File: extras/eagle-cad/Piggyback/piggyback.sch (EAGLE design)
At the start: 2 parts

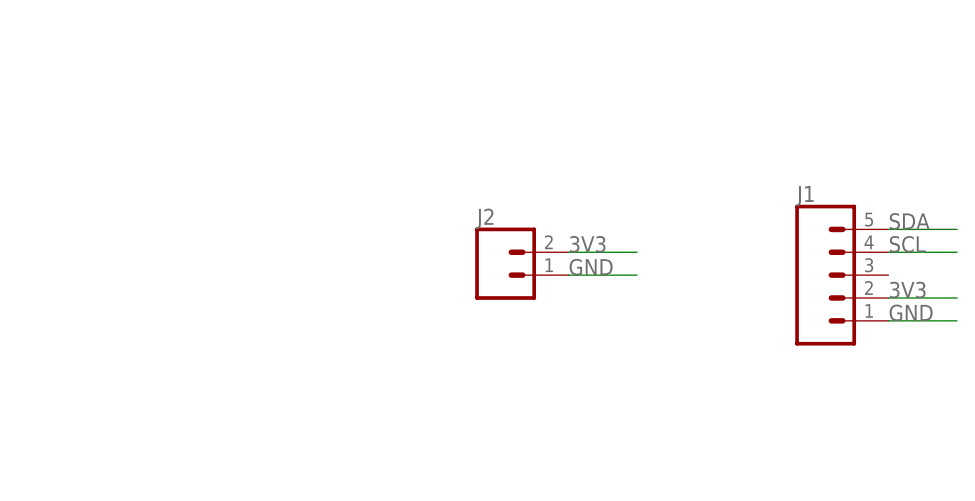
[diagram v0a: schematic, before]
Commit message: Added RX to piggyback board [Issue 134]
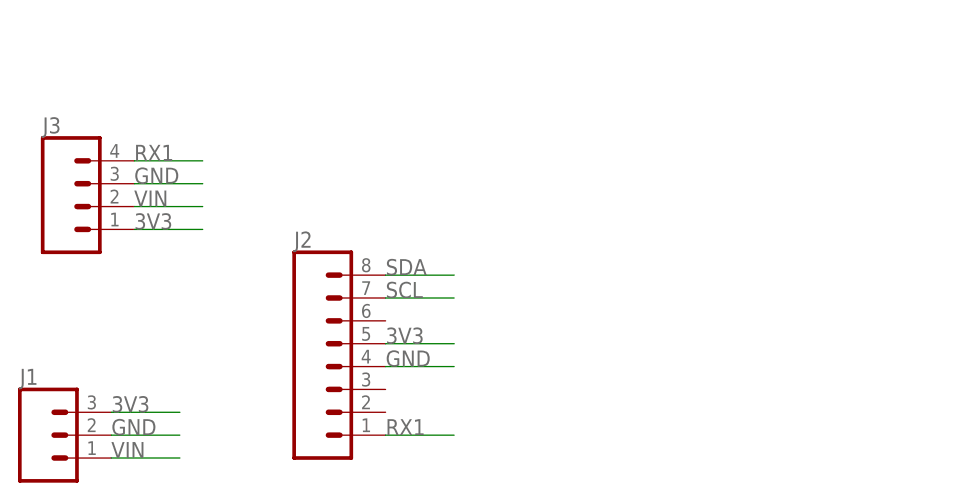
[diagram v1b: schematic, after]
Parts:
- added J3: (no value), SparkFun-Connectors:CONN_041X04_NO_SILK
- J1: device SparkFun-Connectors:CONN_05NO_SILK -> SparkFun-Connectors:CONN_031X03_NO_SILK
- J2: device SparkFun-Connectors:CONN_021X02_NO_SILK -> SparkFun-Connectors:CONN_08NO_SILK_FEMALE_PTH
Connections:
- new net RX1: J2.1, J3.4
- new net VIN: J1.1, J3.2
- net 3V3: now also J1.3, J2.5, J3.1; no longer J1.2, J2.2
- net GND: now also J1.2, J2.4, J3.3; no longer J1.1, J2.1
- net SCL: now also J2.7; no longer J1.4
- net SDA: now also J2.8; no longer J1.5
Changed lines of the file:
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@@
 </classes>
 <parts>
-<part name="J2" library="SparkFun-Connectors" deviceset="CONN_02" device="1X02_NO_SILK"/>
-<part name="J1" library="SparkFun-Connectors" deviceset="CONN_05" device="NO_SILK"/>
+<part name="J1" library="SparkFun-Connectors" deviceset="CONN_03" device="1X03_NO_SILK"/>
+<part name="J2" library="SparkFun-Connectors" deviceset="CONN_08" device="NO_SILK_FEMALE_PTH"/>
+<part name="J3" library="SparkFun-Connectors" deviceset="CONN_04" device="1X04_NO_SILK"/>
 </parts>
 <sheets>
@@
 </plain>
 <instances>
-<instance part="J2" gate="G$1" x="-68.58" y="15.24" smashed="yes">
-<attribute name="VALUE" x="-71.12" y="10.414" size="1.778" layer="96" font="vector"/>
-<attribute name="NAME" x="-71.12" y="20.828" size="1.778" layer="95" font="vector"/>
+<instance part="J1" gate="J$1" x="-119.38" y="-2.54" smashed="yes">
+<attribute name="VALUE" x="-121.92" y="-9.906" size="1.778" layer="96" font="vector"/>
+<attribute name="NAME" x="-121.92" y="3.048" size="1.778" layer="95" font="vector"/>
 </instance>
-<instance part="J1" gate="G$1" x="-33.02" y="15.24" smashed="yes">
-<attribute name="VALUE" x="-35.56" y="5.334" size="1.778" layer="96" font="vector"/>
-<attribute name="NAME" x="-35.56" y="23.368" size="1.778" layer="95" font="vector"/>
+<instance part="J2" gate="G$1" x="-86.36" y="5.08" smashed="yes">
+<attribute name="VALUE" x="-91.44" y="-7.366" size="1.778" layer="96" font="vector"/>
+<attribute name="NAME" x="-91.44" y="18.288" size="1.778" layer="95" font="vector"/>
+</instance>
+<instance part="J3" gate="J1" x="-114.3" y="22.86" smashed="yes">
+<attribute name="VALUE" x="-119.38" y="15.494" size="1.778" layer="96" font="vector"/>
+<attribute name="NAME" x="-119.38" y="30.988" size="1.778" layer="95" font="vector"/>
 </instance>
 </instances>
@@
 </busses>
 <nets>
+<net name="VIN" class="0">
+<segment>
+<pinref part="J1" gate="J$1" pin="1"/>
+<wire x1="-111.76" y1="-5.08" x2="-104.14" y2="-5.08" width="0.1524" layer="91"/>
+<label x="-111.76" y="-5.08" size="1.778" layer="95"/>
+</segment>
+<segment>
+<pinref part="J3" gate="J1" pin="2"/>
+<wire x1="-109.22" y1="22.86" x2="-101.6" y2="22.86" width="0.1524" layer="91"/>
+<label x="-109.22" y="22.86" size="1.778" layer="95"/>
+</segment>
+</net>
 <net name="GND" class="0">
 <segment>
-<pinref part="J2" gate="G$1" pin="1"/>
-<wire x1="-60.96" y1="15.24" x2="-53.34" y2="15.24" width="0.1524" layer="91"/>
-<label x="-60.96" y="15.24" size="1.778" layer="95"/>
+<pinref part="J1" gate="J$1" pin="2"/>
+<wire x1="-111.76" y1="-2.54" x2="-104.14" y2="-2.54" width="0.1524" layer="91"/>
+<label x="-111.76" y="-2.54" size="1.778" layer="95"/>
 </segment>
 <segment>
-<pinref part="J1" gate="G$1" pin="1"/>
-<wire x1="-25.4" y1="10.16" x2="-17.78" y2="10.16" width="0.1524" layer="91"/>
-<label x="-25.4" y="10.16" size="1.778" layer="95"/>
+<pinref part="J2" gate="G$1" pin="4"/>
+<wire x1="-81.28" y1="5.08" x2="-73.66" y2="5.08" width="0.1524" layer="91"/>
+<label x="-81.28" y="5.08" size="1.778" layer="95"/>
+</segment>
+<segment>
+<pinref part="J3" gate="J1" pin="3"/>
+<wire x1="-109.22" y1="25.4" x2="-101.6" y2="25.4" width="0.1524" layer="91"/>
+<label x="-109.22" y="25.4" size="1.778" layer="95"/>
 </segment>
 </net>
 <net name="3V3" class="0">
 <segment>
-<pinref part="J2" gate="G$1" pin="2"/>
-<wire x1="-60.96" y1="17.78" x2="-53.34" y2="17.78" width="0.1524" layer="91"/>
-<label x="-60.96" y="17.78" size="1.778" layer="95"/>
+<pinref part="J1" gate="J$1" pin="3"/>
+<wire x1="-111.76" y1="0" x2="-104.14" y2="0" width="0.1524" layer="91"/>
+<label x="-111.76" y="0" size="1.778" layer="95"/>
 </segment>
 <segment>
-<pinref part="J1" gate="G$1" pin="2"/>
-<wire x1="-25.4" y1="12.7" x2="-17.78" y2="12.7" width="0.1524" layer="91"/>
-<label x="-25.4" y="12.7" size="1.778" layer="95"/>
+<pinref part="J2" gate="G$1" pin="5"/>
+<wire x1="-81.28" y1="7.62" x2="-73.66" y2="7.62" width="0.1524" layer="91"/>
+<label x="-81.28" y="7.62" size="1.778" layer="95"/>
+</segment>
+<segment>
+<pinref part="J3" gate="J1" pin="1"/>
+<wire x1="-109.22" y1="20.32" x2="-101.6" y2="20.32" width="0.1524" layer="91"/>
+<label x="-109.22" y="20.32" size="1.778" layer="95"/>
+</segment>
+</net>
+<net name="RX1" class="0">
+<segment>
+<pinref part="J2" gate="G$1" pin="1"/>
+<wire x1="-81.28" y1="-2.54" x2="-73.66" y2="-2.54" width="0.1524" layer="91"/>
+<label x="-81.28" y="-2.54" size="1.778" layer="95"/>
+</segment>
+<segment>
+<pinref part="J3" gate="J1" pin="4"/>
+<wire x1="-109.22" y1="27.94" x2="-101.6" y2="27.94" width="0.1524" layer="91"/>
+<label x="-109.22" y="27.94" size="1.778" layer="95"/>
 </segment>
 </net>
 <net name="SCL" class="0">
 <segment>
-<pinref part="J1" gate="G$1" pin="4"/>
-<wire x1="-25.4" y1="17.78" x2="-17.78" y2="17.78" width="0.1524" layer="91"/>
-<label x="-25.4" y="17.78" size="1.778" layer="95"/>
+<pinref part="J2" gate="G$1" pin="7"/>
+<wire x1="-81.28" y1="12.7" x2="-73.66" y2="12.7" width="0.1524" layer="91"/>
+<label x="-81.28" y="12.7" size="1.778" layer="95"/>
 </segment>
 </net>
 <net name="SDA" class="0">
 <segment>
-<pinref part="J1" gate="G$1" pin="5"/>
-<wire x1="-25.4" y1="20.32" x2="-17.78" y2="20.32" width="0.1524" layer="91"/>
-<label x="-25.4" y="20.32" size="1.778" layer="95"/>
+<pinref part="J2" gate="G$1" pin="8"/>
+<wire x1="-81.28" y1="15.24" x2="-73.66" y2="15.24" width="0.1524" layer="91"/>
+<label x="-81.28" y="15.24" size="1.778" layer="95"/>
 </segment>
 </net>

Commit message: More Butterfly Piggyback board work
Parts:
- J1: device SparkFun-Connectors:CONN_031X03_NO_SILK -> SparkFun-Connectors:CONN_09NO_SILK
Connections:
- new net INT: J1.9, J2.3
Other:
- moved on the sheet: J3
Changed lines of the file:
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@@
 <?xml version="1.0" encoding="utf-8"?>
 <!DOCTYPE eagle SYSTEM "eagle.dtd">
-<eagle version="9.6.2">
+<eagle version="9.1.1">
 <drawing>
 <settings>
@@
 </classes>
 <parts>
-<part name="J1" library="SparkFun-Connectors" deviceset="CONN_03" device="1X03_NO_SILK"/>
 <part name="J2" library="SparkFun-Connectors" deviceset="CONN_08" device="NO_SILK_FEMALE_PTH"/>
 <part name="J3" library="SparkFun-Connectors" deviceset="CONN_04" device="1X04_NO_SILK"/>
+<part name="J1" library="SparkFun-Connectors" deviceset="CONN_09" device="NO_SILK"/>
 </parts>
 <sheets>
@@
 </plain>
 <instances>
-<instance part="J1" gate="J$1" x="-119.38" y="-2.54" smashed="yes">
-<attribute name="VALUE" x="-121.92" y="-9.906" size="1.778" layer="96" font="vector"/>
-<attribute name="NAME" x="-121.92" y="3.048" size="1.778" layer="95" font="vector"/>
-</instance>
 <instance part="J2" gate="G$1" x="-86.36" y="5.08" smashed="yes">
 <attribute name="VALUE" x="-91.44" y="-7.366" size="1.778" layer="96" font="vector"/>
 <attribute name="NAME" x="-91.44" y="18.288" size="1.778" layer="95" font="vector"/>
 </instance>
-<instance part="J3" gate="J1" x="-114.3" y="22.86" smashed="yes">
-<attribute name="VALUE" x="-119.38" y="15.494" size="1.778" layer="96" font="vector"/>
-<attribute name="NAME" x="-119.38" y="30.988" size="1.778" layer="95" font="vector"/>
+<instance part="J3" gate="J1" x="-86.36" y="33.02" smashed="yes">
+<attribute name="VALUE" x="-91.44" y="25.654" size="1.778" layer="96" font="vector"/>
+<attribute name="NAME" x="-91.44" y="41.148" size="1.778" layer="95" font="vector"/>
 </instance>
+<instance part="J1" gate="J1" x="-116.84" y="5.08"/>
 </instances>
 <busses>
@@
 <net name="VIN" class="0">
 <segment>
-<pinref part="J1" gate="J$1" pin="1"/>
-<wire x1="-111.76" y1="-5.08" x2="-104.14" y2="-5.08" width="0.1524" layer="91"/>
-<label x="-111.76" y="-5.08" size="1.778" layer="95"/>
-</segment>
-<segment>
 <pinref part="J3" gate="J1" pin="2"/>
-<wire x1="-109.22" y1="22.86" x2="-101.6" y2="22.86" width="0.1524" layer="91"/>
-<label x="-109.22" y="22.86" size="1.778" layer="95"/>
+<wire x1="-81.28" y1="33.02" x2="-73.66" y2="33.02" width="0.1524" layer="91"/>
+<label x="-81.28" y="33.02" size="1.778" layer="95"/>
+</segment>
+<segment>
+<pinref part="J1" gate="J1" pin="1"/>
+<wire x1="-106.68" y1="-5.08" x2="-99.06" y2="-5.08" width="0.1524" layer="91"/>
+<label x="-106.68" y="-5.08" size="1.778" layer="95"/>
 </segment>
 </net>
 <net name="GND" class="0">
-<segment>
-<pinref part="J1" gate="J$1" pin="2"/>
-<wire x1="-111.76" y1="-2.54" x2="-104.14" y2="-2.54" width="0.1524" layer="91"/>
-<label x="-111.76" y="-2.54" size="1.778" layer="95"/>
-</segment>
 <segment>
 <pinref part="J2" gate="G$1" pin="4"/>
@@
 <segment>
 <pinref part="J3" gate="J1" pin="3"/>
-<wire x1="-109.22" y1="25.4" x2="-101.6" y2="25.4" width="0.1524" layer="91"/>
-<label x="-109.22" y="25.4" size="1.778" layer="95"/>
+<wire x1="-81.28" y1="35.56" x2="-73.66" y2="35.56" width="0.1524" layer="91"/>
+<label x="-81.28" y="35.56" size="1.778" layer="95"/>
+</segment>
+<segment>
+<pinref part="J1" gate="J1" pin="2"/>
+<wire x1="-106.68" y1="-2.54" x2="-99.06" y2="-2.54" width="0.1524" layer="91"/>
+<label x="-106.68" y="-2.54" size="1.778" layer="95"/>
 </segment>
 </net>
 <net name="3V3" class="0">
-<segment>
-<pinref part="J1" gate="J$1" pin="3"/>
-<wire x1="-111.76" y1="0" x2="-104.14" y2="0" width="0.1524" layer="91"/>
-<label x="-111.76" y="0" size="1.778" layer="95"/>
-</segment>
 <segment>
 <pinref part="J2" gate="G$1" pin="5"/>
@@
 <segment>
 <pinref part="J3" gate="J1" pin="1"/>
-<wire x1="-109.22" y1="20.32" x2="-101.6" y2="20.32" width="0.1524" layer="91"/>
-<label x="-109.22" y="20.32" size="1.778" layer="95"/>
+<wire x1="-81.28" y1="30.48" x2="-73.66" y2="30.48" width="0.1524" layer="91"/>
+<label x="-81.28" y="30.48" size="1.778" layer="95"/>
+</segment>
+<segment>
+<pinref part="J1" gate="J1" pin="3"/>
+<wire x1="-106.68" y1="0" x2="-99.06" y2="0" width="0.1524" layer="91"/>
+<label x="-106.68" y="0" size="1.778" layer="95"/>
 </segment>
 </net>
@@
 <segment>
 <pinref part="J3" gate="J1" pin="4"/>
-<wire x1="-109.22" y1="27.94" x2="-101.6" y2="27.94" width="0.1524" layer="91"/>
-<label x="-109.22" y="27.94" size="1.778" layer="95"/>
+<wire x1="-81.28" y1="38.1" x2="-73.66" y2="38.1" width="0.1524" layer="91"/>
+<label x="-81.28" y="38.1" size="1.778" layer="95"/>
 </segment>
 </net>
@@
 </segment>
 </net>
+<net name="INT" class="0">
+<segment>
+<pinref part="J2" gate="G$1" pin="3"/>
+<wire x1="-81.28" y1="2.54" x2="-73.66" y2="2.54" width="0.1524" layer="91"/>
+<label x="-81.28" y="2.54" size="1.778" layer="95"/>
+</segment>
+<segment>
+<pinref part="J1" gate="J1" pin="9"/>
+<wire x1="-106.68" y1="15.24" x2="-99.06" y2="15.24" width="0.1524" layer="91"/>
+<label x="-106.68" y="15.24" size="1.778" layer="95"/>
+</segment>
+</net>
